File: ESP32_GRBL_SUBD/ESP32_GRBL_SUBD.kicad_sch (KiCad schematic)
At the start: 63 parts, among them J1 DB25_Female_MountingHoles, J10 Screw_Terminal_01x02, J11 Screw_Terminal_01x02, J12 Screw_Terminal_01x02, J13 Screw_Terminal_01x02, J2 Micro_SD_Card, J3 Conn_01x19_Female, J4 Conn_01x19_Female, J5 Screw_Terminal_01x02, J6 Screw_Terminal_01x02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

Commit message: One unused output pin resistor to GND added. The logic level converter shouldnt be floating
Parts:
- added R42: 0R, Resistor_SMD:R_0603_1608Metric, symbol Device:R
- gave numbers to parts that had none: 2
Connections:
- net ENABLE_3V3: now also R42.2
- net GND: now also R42.1
- net ENABLE renamed BOOST
- net OUT1 renamed ENABLE_SPINDEL
- net OUT2 renamed /SLEEP
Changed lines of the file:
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@@
   (junction (at 207.01 251.46) (diameter 0) (color 0 0 0 0)
   )
+  (junction (at 274.32 99.06) (diameter 0) (color 0 0 0 0)
+  )
   (junction (at 256.54 88.9) (diameter 0) (color 0 0 0 0)
   )
@@
     (stroke (width 0) (type default) (color 0 0 0 0))
   )
+  (wire (pts (xy 228.6 99.06) (xy 228.6 88.9))
+    (stroke (width 0) (type default) (color 0 0 0 0))
+  )
   (wire (pts (xy 149.86 77.47) (xy 177.8 77.47))
     (stroke (width 0) (type default) (color 0 0 0 0))
@@
     (stroke (width 0) (type default) (color 0 0 0 0))
   )
+  (wire (pts (xy 238.76 99.06) (xy 228.6 99.06))
+    (stroke (width 0) (type default) (color 0 0 0 0))
+  )
   (wire (pts (xy 46.99 35.56) (xy 36.83 35.56))
     (stroke (width 0) (type default) (color 0 0 0 0))
@@
     (stroke (width 0) (type default) (color 0 0 0 0))
   )
+  (wire (pts (xy 246.38 99.06) (xy 274.32 99.06))
+    (stroke (width 0) (type default) (color 0 0 0 0))
+  )
   (wire (pts (xy 280.67 106.68) (xy 190.5 106.68))
     (stroke (width 0) (type default) (color 0 0 0 0))
@@
     (effects (font (size 1.27 1.27)) (justify left bottom))
   )
-  (label "OUT1" (at 353.06 31.75 0)
+  (label "ENABLE_SPINDEL" (at 353.06 31.75 0)
     (effects (font (size 1.27 1.27)) (justify left bottom))
   )
@@
     (effects (font (size 1.27 1.27)) (justify left bottom))
   )
-  (label "OUT1" (at 307.34 93.98 0)
+  (label "ENABLE_SPINDEL" (at 307.34 93.98 0)
     (effects (font (size 1.27 1.27)) (justify left bottom))
   )
@@
     (effects (font (size 1.27 1.27)) (justify left bottom))
   )
-  (label "OUT2" (at 307.34 88.9 0)
+  (label "{slash}SLEEP" (at 307.34 88.9 0)
     (effects (font (size 1.27 1.27)) (justify left bottom))
   )
@@
     (effects (font (size 1.27 1.27)) (justify left bottom))
   )
-  (label "OUT2" (at 353.06 49.53 0)
+  (label "{slash}SLEEP" (at 353.06 49.53 0)
     (effects (font (size 1.27 1.27)) (justify left bottom))
   )
-  (label "ENABLE" (at 307.34 91.44 0)
+  (label "BOOST" (at 307.34 91.44 0)
     (effects (font (size 1.27 1.27)) (justify left bottom))
   )
@@
     (effects (font (size 1.27 1.27)) (justify left bottom))
   )
-  (label "ENABLE" (at 353.06 44.45 0)
+  (label "BOOST" (at 353.06 44.45 0)
     (effects (font (size 1.27 1.27)) (justify left bottom))
   )
@@
   (symbol (lib_id "Connector:Conn_01x19_Female") (at 50.8 137.16 0) (mirror x) (unit 1)
     (in_bom yes) (on_board yes)
-    (property "Reference" "" (id 0) (at 48.0568 108.585 0))
+    (property "Reference" "J3a1" (id 0) (at 48.0568 108.585 0))
     (property "Value" "Conn_01x19_Female" (id 1) (at 48.0568 110.8964 0))
     (property "Footprint" "Connector_PinSocket_2.54mm:PinSocket_1x19_P2.54mm_Vertical" (id 2) (at 50.8 137.16 0)
@@
   (symbol (lib_id "Connector:Conn_01x19_Female") (at 77.47 137.16 180) (unit 1)
     (in_bom yes) (on_board yes)
-    (property "Reference" "" (id 0) (at 80.2132 108.585 0))
+    (property "Reference" "J4a1" (id 0) (at 80.2132 108.585 0))
     (property "Value" "Conn_01x19_Female" (id 1) (at 80.2132 110.8964 0))
     (property "Footprint" "Connector_PinSocket_2.54mm:PinSocket_1x19_P2.54mm_Vertical" (id 2) (at 77.47 137.16 0)
@@
   (symbol (lib_id "ESP32_GRBL_SUBD-rescue:+3.3V-power") (at 36.83 24.13 0) (unit 1)
     (in_bom yes) (on_board yes)
-    (property "Reference" "" (id 0) (at 36.83 27.94 0)
+    (property "Reference" "#PWR0105" (id 0) (at 36.83 27.94 0)
       (effects (font (size 1.27 1.27)) hide)
     )
@@
   (symbol (lib_id "ESP32_GRBL_SUBD-rescue:+3.3V-power") (at 35.56 105.41 0) (unit 1)
     (in_bom yes) (on_board yes)
-    (property "Reference" "" (id 0) (at 35.56 109.22 0)
+    (property "Reference" "#PWR0106" (id 0) (at 35.56 109.22 0)
       (effects (font (size 1.27 1.27)) hide)
     )
@@
   (symbol (lib_id "ESP32_GRBL_SUBD-rescue:+3.3V-power") (at 207.01 247.65 0) (unit 1)
     (in_bom yes) (on_board yes)
-    (property "Reference" "" (id 0) (at 207.01 251.46 0)
+    (property "Reference" "#PWR0111" (id 0) (at 207.01 251.46 0)
       (effects (font (size 1.27 1.27)) hide)
     )
@@
   (symbol (lib_id "ESP32_GRBL_SUBD-rescue:+3.3V-power") (at 87.63 238.76 0) (unit 1)
     (in_bom yes) (on_board yes)
-    (property "Reference" "" (id 0) (at 87.63 242.57 0)
+    (property "Reference" "#PWR026" (id 0) (at 87.63 242.57 0)
       (effects (font (size 1.27 1.27)) hide)
     )
@@
   (symbol (lib_id "ESP32_GRBL_SUBD-rescue:+3.3V-power") (at 29.21 234.95 0) (unit 1)
     (in_bom yes) (on_board yes)
-    (property "Reference" "" (id 0) (at 29.21 238.76 0)
+    (property "Reference" "#PWR012" (id 0) (at 29.21 238.76 0)
       (effects (font (size 1.27 1.27)) hide)
     )
@@
   (symbol (lib_id "ESP32_GRBL_SUBD-rescue:+3.3V-power") (at 36.83 234.95 0) (unit 1)
     (in_bom yes) (on_board yes)
-    (property "Reference" "" (id 0) (at 36.83 238.76 0)
+    (property "Reference" "#PWR015" (id 0) (at 36.83 238.76 0)
       (effects (font (size 1.27 1.27)) hide)
     )
@@
   (symbol (lib_id "ESP32_GRBL_SUBD-rescue:+3.3V-power") (at 44.45 234.95 0) (unit 1)
     (in_bom yes) (on_board yes)
-    (property "Reference" "" (id 0) (at 44.45 238.76 0)
+    (property "Reference" "#PWR016" (id 0) (at 44.45 238.76 0)
       (effects (font (size 1.27 1.27)) hide)
     )
@@
   (symbol (lib_id "ESP32_GRBL_SUBD-rescue:+3.3V-power") (at 52.07 234.95 0) (unit 1)
     (in_bom yes) (on_board yes)
-    (property "Reference" "" (id 0) (at 52.07 238.76 0)
+    (property "Reference" "#PWR017" (id 0) (at 52.07 238.76 0)
       (effects (font (size 1.27 1.27)) hide)
     )
@@
   (symbol (lib_id "ESP32_GRBL_SUBD-rescue:+3.3V-power") (at 59.69 234.95 0) (unit 1)
     (in_bom yes) (on_board yes)
-    (property "Reference" "" (id 0) (at 59.69 238.76 0)
+    (property "Reference" "#PWR018" (id 0) (at 59.69 238.76 0)
       (effects (font (size 1.27 1.27)) hide)
     )
@@
   (symbol (lib_id "ESP32_GRBL_SUBD-rescue:+3.3V-power") (at 67.31 234.95 0) (unit 1)
     (in_bom yes) (on_board yes)
-    (property "Reference" "" (id 0) (at 67.31 238.76 0)
+    (property "Reference" "#PWR019" (id 0) (at 67.31 238.76 0)
       (effects (font (size 1.27 1.27)) hide)
     )
@@
   (symbol (lib_id "ESP32_GRBL_SUBD-rescue:+3.3V-power") (at 93.98 214.63 0) (unit 1)
     (in_bom yes) (on_board yes)
-    (property "Reference" "" (id 0) (at 93.98 218.44 0)
+    (property "Reference" "#PWR048" (id 0) (at 93.98 218.44 0)
       (effects (font (size 1.27 1.27)) hide)
     )
@@
   (symbol (lib_id "ESP32_GRBL_SUBD-rescue:+3.3V-power") (at 138.43 33.02 0) (unit 1)
     (in_bom yes) (on_board yes)
-    (property "Reference" "" (id 0) (at 138.43 36.83 0)
+    (property "Reference" "#PWR050" (id 0) (at 138.43 36.83 0)
       (effects (font (size 1.27 1.27)) hide)
     )
@@
   (symbol (lib_id "ESP32_GRBL_SUBD-rescue:+3.3V-power") (at 82.55 214.63 0) (unit 1)
     (in_bom yes) (on_board yes)
-    (property "Reference" "" (id 0) (at 82.55 218.44 0)
+    (property "Reference" "#PWR046" (id 0) (at 82.55 218.44 0)
       (effects (font (size 1.27 1.27)) hide)
     )
@@
     (pin "2")
   )
+  (symbol (lib_id "Device:R") (at 242.57 99.06 270) (unit 1)
+    (in_bom yes) (on_board yes)
+    (property "Reference" "R42" (id 0) (at 243.7384 100.838 0)
+      (effects (font (size 1.27 1.27)) (justify left))
+    )
+    (property "Value" "0R" (id 1) (at 241.427 100.838 0)
+      (effects (font (size 1.27 1.27)) (justify left))
+    )
+    (property "Footprint" "Resistor_SMD:R_0603_1608Metric" (id 2) (at 242.57 97.282 90)
+      (effects (font (size 1.27 1.27)) hide)
+    )
+    (property "Datasheet" "~" (id 3) (at 242.57 99.06 0)
+      (effects (font (size 1.27 1.27)) hide)
+    )
+    (pin "1")
+    (pin "2")
+  )
   (symbol (lib_id "Device:R") (at 184.15 82.55 0) (unit 1)
     (in_bom yes) (on_board yes)
@@
       (reference "R41") (unit 1) (value "dnp") (footprint "Resistor_SMD:R_0603_1608Metric")
     )
+    (path "/6f7d2e2d-ab5c-405a-a7ee-a3211d67f7b6"
+      (reference "R42") (unit 1) (value "0R") (footprint "Resistor_SMD:R_0603_1608Metric")
+    )
     (path "/00000000-0000-0000-0000-00005eb34bbe"

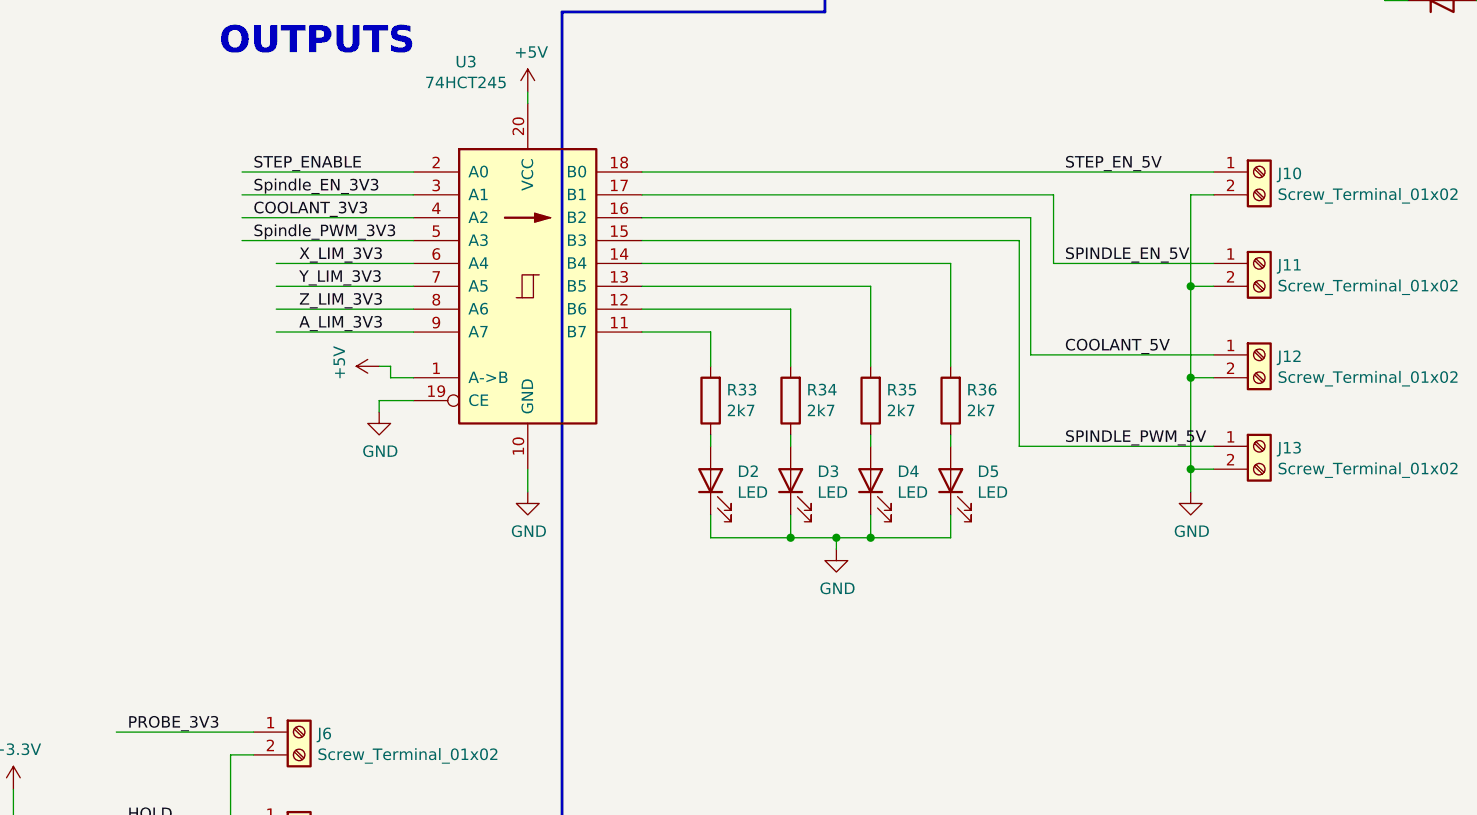
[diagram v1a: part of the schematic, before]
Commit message: mapped UART0 to screw header
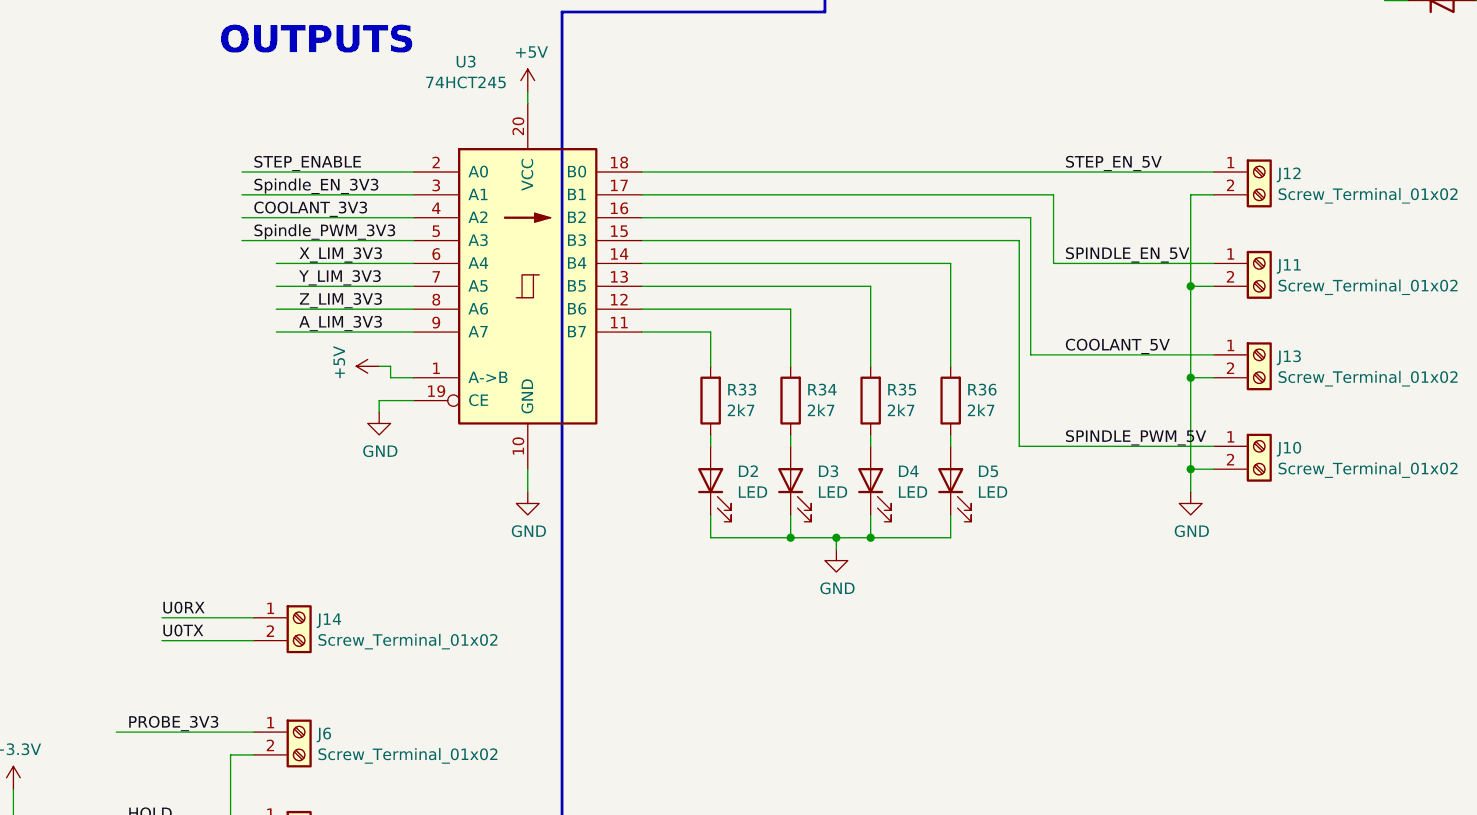
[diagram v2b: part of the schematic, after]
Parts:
- added J14: Screw_Terminal_01x02, TerminalBlock_MetzConnect:TerminalBlock_MetzConnect_Type055_RT01502HDWU_1x02_P5.00mm_Horizontal, symbol Connector:Screw_Terminal_01x02
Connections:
- net COOLANT_5V: now also J13.1 (Pin_1); no longer J12.1 (Pin_1)
- net SPINDLE_PWM_5V: now also J10.1 (Pin_1); no longer J13.1 (Pin_1)
- net STEP_EN_5V: now also J12.1 (Pin_1); no longer J10.1 (Pin_1)
- net U0RX: now also J14.1 (Pin_1)
- net U0TX: now also J14.2 (Pin_2)
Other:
- moved on the sheet: J10, J12, J13

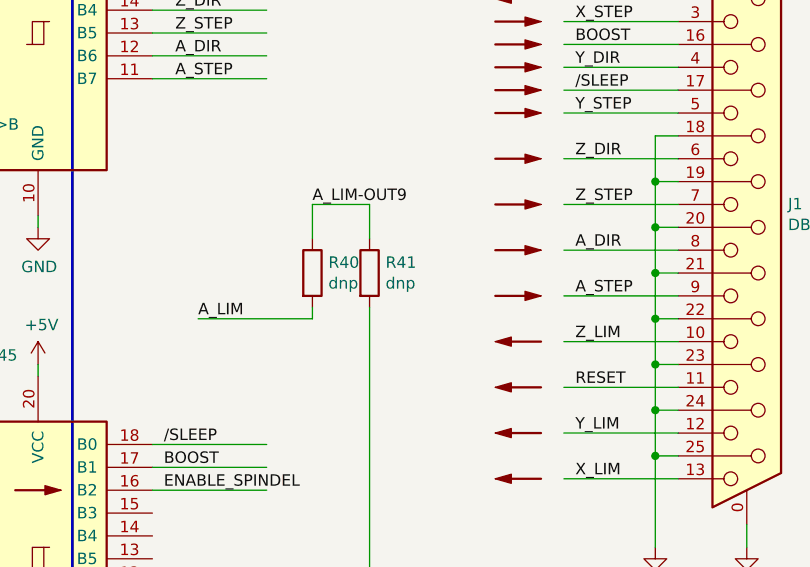
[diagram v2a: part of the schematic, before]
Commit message: changed value of Resistor to match my actual soldered PCB
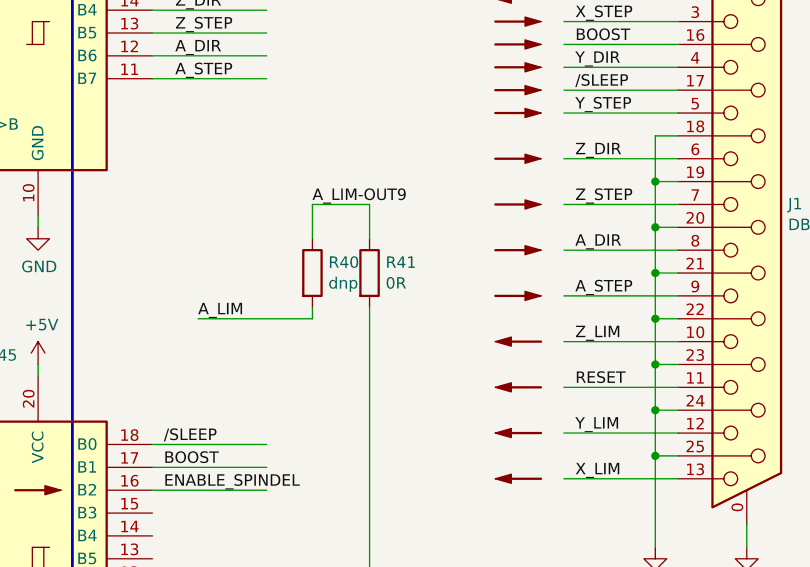
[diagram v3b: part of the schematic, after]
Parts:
- R41: value dnp -> 0R
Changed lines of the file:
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@@
       (effects (font (size 1.27 1.27)) (justify left))
     )
-    (property "Value" "dnp" (id 1) (at 331.978 70.993 0)
+    (property "Value" "0R" (id 1) (at 331.978 70.993 0)
       (effects (font (size 1.27 1.27)) (justify left))
     )
@@
     )
     (path "/372ca174-dd9f-4c57-bc55-279c6f8b4e3a"
-      (reference "R41") (unit 1) (value "dnp") (footprint "Resistor_SMD:R_0603_1608Metric")
+      (reference "R41") (unit 1) (value "0R") (footprint "Resistor_SMD:R_0603_1608Metric")
     )
     (path "/6f7d2e2d-ab5c-405a-a7ee-a3211d67f7b6"
